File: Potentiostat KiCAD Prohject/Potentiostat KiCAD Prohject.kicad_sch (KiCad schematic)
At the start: 30 parts, among them K1 DIPxx-1Axx-12xD, U1 OPA2277, U2 TL074, U3 RP2040, U4 OPA2277, U5 INA128, U7 INA128, U8 REF3033, U9 INA128

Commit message: completed ESP32 design
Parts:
- removed U3: RP2040, Package_DFN_QFN:QFN-56-1EP_7x7mm_P0.4mm_EP3.2x3.2mm, symbol MCU_RaspberryPi:RP2040
- added J1: USB_B_Micro, symbol Connector:USB_B_Micro
- added U10: ADS1115IDGS, Package_SO:TSSOP-10_3x3mm_P0.5mm, symbol Analog_ADC:ADS1115IDGS
- added U11, U6: MCP4725xxx-xCH, Package_TO_SOT_SMD:SOT-23-6, symbol Analog_DAC:MCP4725xxx-xCH
- added U12: RT9080-33GJ5, TSOT-23-5_RIT, symbol 2025-04-04_01-18-31:RT9080-33GJ5
- added U3: ESP32-S2, Package_DFN_QFN:QFN-56-1EP_7x7mm_P0.4mm_EP4x4mm, symbol MCU_Espressif:ESP32-S2
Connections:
- net GND: now also U10.3 (GND), U11.2 (VSS), U3.57 (GND), U6.2 (VSS), U6.6 (A0)
- net goes to ADC: no longer names the net of R6.1, R7.1, U1.5 (+), U1.7
- net goes to ADC: now also U10.7 (AIN3); no longer D2.1 (K), U9.2 (-), U9.6
- net goes to DAC: no longer names the net of U1.6 (-)
- net goes to DAC: now also U6.1 (VOUT)
- net goes to MCU: no longer names the net of K1.7, K1.8
- net goes to MCU: now also U10.5 (AIN1); no longer R12.2, R5.1
- new net: R12.2, U3.17 (GPIO12)
- new net: D2.1 (K), U10.6 (AIN2), U9.2 (-), U9.6
- new net: R5.1, U11.1 (VOUT)
- new net: U10.9 (SDA), U11.4 (SDA), U3.13 (GPIO8), U6.4 (SDA)
- new net: U10.10 (SCL), U11.5 (SCL), U3.14 (GPIO9), U6.5 (SCL)
- new net: J1.1 (VBUS), U12.1 (VIN)
- new net: J1.2 (D-), U3.25 (GPIO19/USB_D-)
- new net: J1.3 (D+), U3.26 (GPIO20/USB_D+)
- new net: J1.5 (GND), U12.2 (GND)
- new net: U12.5 (VOUT), U3.45 (VDD3P3_CPU)
- new net: U3.1 (VDDA), U3.51 (VDDA), U3.54 (VDDA)
- new net: U3.3 (VDD3P3), U3.4 (VDD3P3)
- new net VCC: U10.8 (VDD), U11.3 (VDD), U11.6 (A0), U6.3 (VDD)

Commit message: add microcontroller stuff
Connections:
- net GND: now also J1.5 (GND), U12.2 (GND)
- net at U12.5 (VOUT): now also U3.3 (VDD3P3), U3.4 (VDD3P3); no longer U3.45 (VDD3P3_CPU)
- no-connect marks 12 -> 65

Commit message: esp32 solo and cleanup
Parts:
- removed J1: USB_B_Micro, symbol Connector:USB_B_Micro
- removed U12: RT9080-33GJ5, TSOT-23-5_RIT, symbol 2025-04-04_01-18-31:RT9080-33GJ5
- removed U3: ESP32-S2, Package_DFN_QFN:QFN-56-1EP_7x7mm_P0.4mm_EP4x4mm, symbol MCU_Espressif:ESP32-S2
- added C2: 100nF, Capacitor_SMD:C_0805_2012Metric_Pad1.18x1.45mm_HandSolder, symbol Device:C
- added C3: 10uF, Capacitor_SMD:C_0805_2012Metric_Pad1.18x1.45mm_HandSolder, symbol Device:C
- added C4, C6: .1uF, Capacitor_SMD:C_0805_2012Metric_Pad1.18x1.45mm_HandSolder, symbol Device:C
- added C5: 1uF, Capacitor_SMD:C_0805_2012Metric_Pad1.18x1.45mm_HandSolder, symbol Device:C
- added J2: USB_C_Receptacle_USB2.0, Connector_USB:USB_C_Receptacle_GCT_USB4105-xx-A_16P_TopMnt_Horizontal, symbol Connector:USB_C_Receptacle_USB2.0
- added R19, R20: 5.1 k, Resistor_SMD:R_0805_2012Metric_Pad1.20x1.40mm_HandSolder, symbol Device:R
- added R21: 10k, Resistor_SMD:R_0805_2012Metric_Pad1.20x1.40mm_HandSolder, symbol Device:R
- added SW1: Reset, symbol Switch:SW_Omron_B3FS
- added SW2: Boot, symbol Switch:SW_Omron_B3FS
- added U13: LD1117S33TR_SOT223, Package_TO_SOT_SMD:SOT-223-3_TabPin2, symbol Regulator_Linear:LD1117S33TR_SOT223
- added U14: ESP32-S2-SOLO, PCM_Espressif:ESP32-S2-SOLO, symbol esp32:ESP32-S2-SOLO
- C1: footprint (none) -> B58031I7504M062:CAPC7851084X4N
- D1: footprint (none) -> LED_SMD:LED_0603_1608Metric
- R1, R10, R11, R13, R14, R15, R16, R17, R18, R2, R3, R4, R5, R6, R7, R8, R9: footprint (none) -> Resistor_THT:R_Axial_DIN0207_L6.3mm_D2.5mm_P7.62mm_Horizontal
- R12: footprint (none) -> footprints:res2_1-1625885-7_TEC
- U1, U4, U5, U7, U9: footprint (none) -> Package_SO:SOIC-8_3.9x4.9mm_P1.27mm
- U2: footprint (none) -> Package_SO:SOIC-14_3.9x8.7mm_P1.27mm
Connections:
- net GND: now also C2.2, C3.2, C4.1, C5.2, C6.2, J2.A1 (GND), J2.A12 (GND), J2.B1 (GND), J2.B12 (GND), J2.S1 (SHIELD), R19.2, R20.1, SW1.1, SW2.2, U13.1 (GND), U14.1 (GND), U14.40 (GND), U14.41 (GND)
- net at R12.2: now also U14.20 (GPIO12/TOUCH12/ADC2_CH1/FSPICLK/FSPIIO6)
- net at R13.2, R15.2, R16.1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: now also R14.1; no longer R14.2
- net I2C_SDA: now reaches U10.9 (SDA), U11.4 (SDA), U6.4 (SDA)
- net I2C_SDA: now also U14.17 (GPIO9/TOUCH9/ADC1_CH8/FSPIHD)
- net I2C_SCL: now reaches U10.10 (SCL), U11.5 (SCL), U6.5 (SCL)
- net I2C_SCL: now also U14.12 (GPIO8/TOUCH8/ADC1_CH7)
- net at R6.1, R7.1, U1.5 (+)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: no longer U10.7 (AIN3)
- net at R13.1, U7.6, U9.3 (+): now also R14.2; no longer R14.1
- new net: C4.2, R21.2, SW1.2, U14.3 (EN)
- new net: SW2.1, U14.27 (GPIO0)
- new net: J2.A5 (CC1), R19.1
- new net: J2.B5 (CC2), R20.2
- new net +3.3V: C3.1, C5.1, C6.1, R21.1, U13.2 (VO), U14.2 (3V3)
- new net +5V: C2.1, J2.A4 (VBUS), J2.A9 (VBUS), J2.B4 (VBUS), J2.B9 (VBUS), U13.3 (VI)
- new net D+: J2.A6 (D+), J2.B6 (D+), U14.14 (GPIO20/U1CTS/ADC2_CH9/CLK_OUT1/USB_D+)
- new net D-: J2.A7 (D-), J2.B7 (D-), U14.13 (GPIO19/U1RTS/ADC2_CH8/CLK_OUT2/USB_D-)
- no-connect marks 65 -> 17
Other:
- note added: "3.3V Supply"
- note added: "ESP32S2"
- note added: "USB_Connector"
- moved on the sheet: D1, R12, R14, U11, U2A, U2B, U2C, U2E, U6

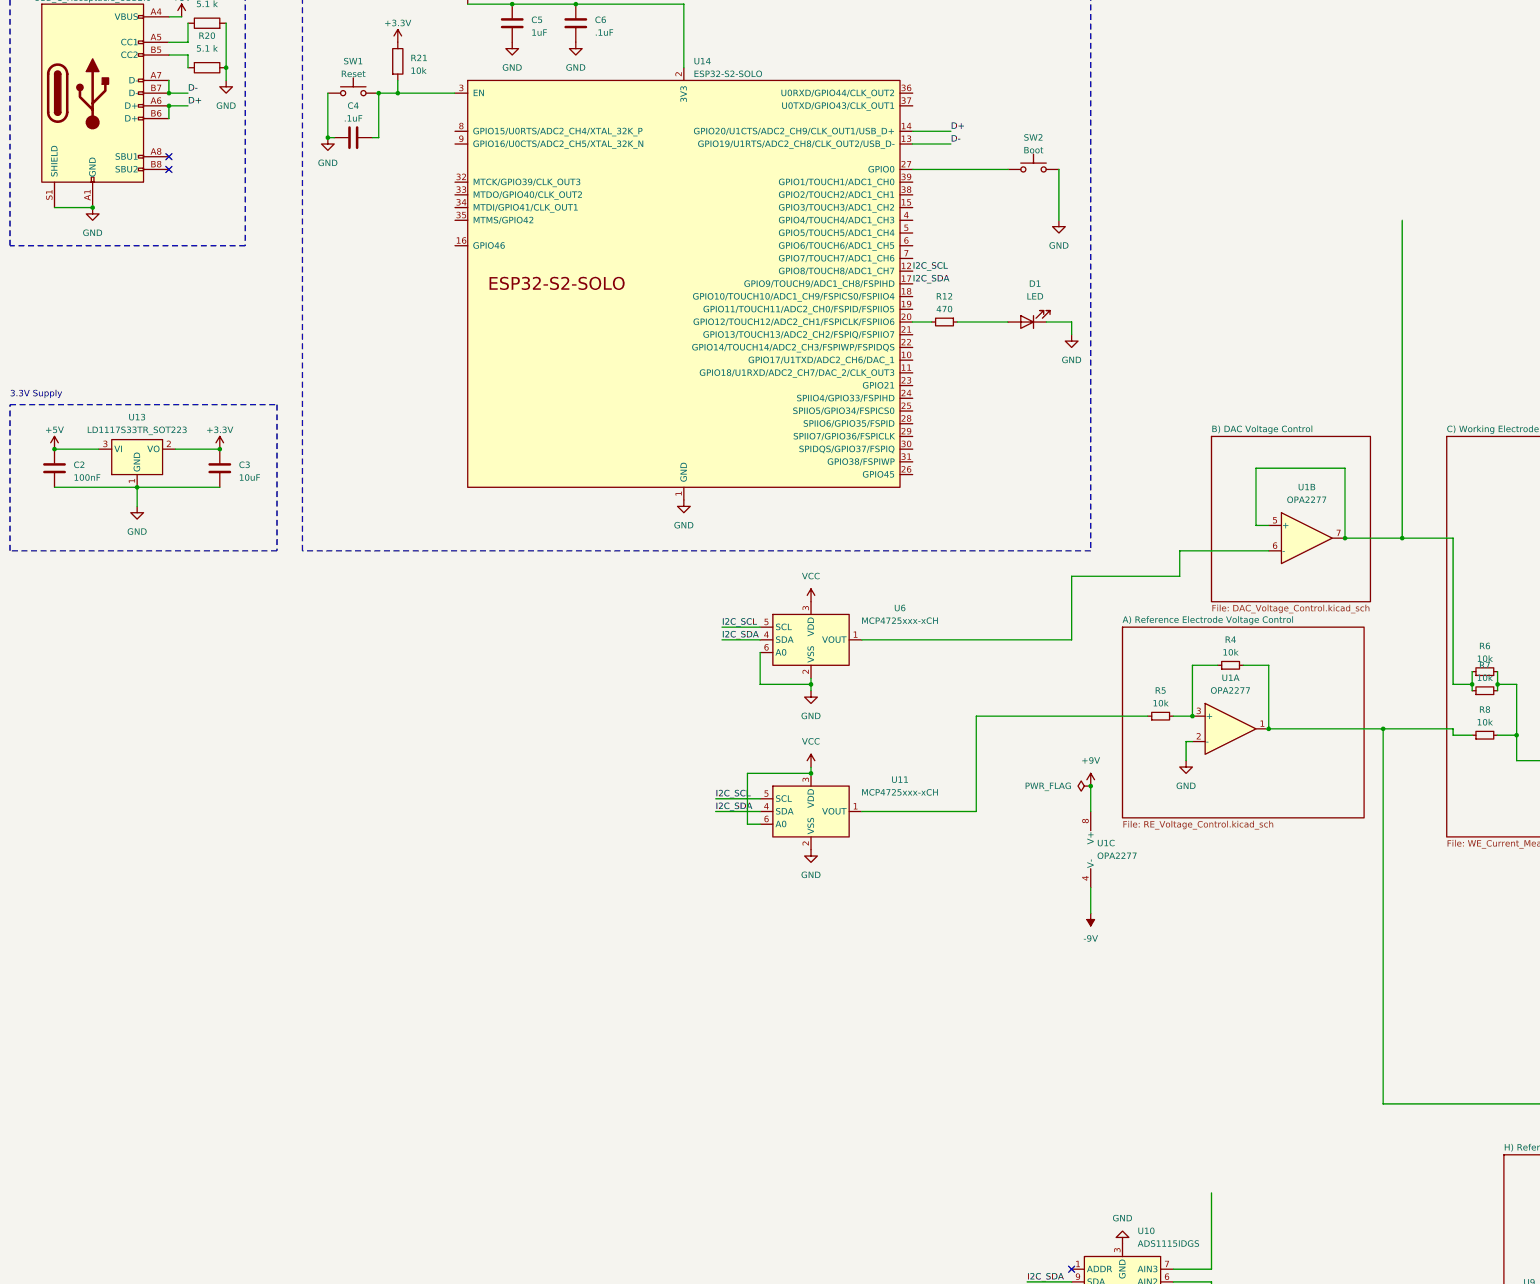
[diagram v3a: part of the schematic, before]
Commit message: updated wires
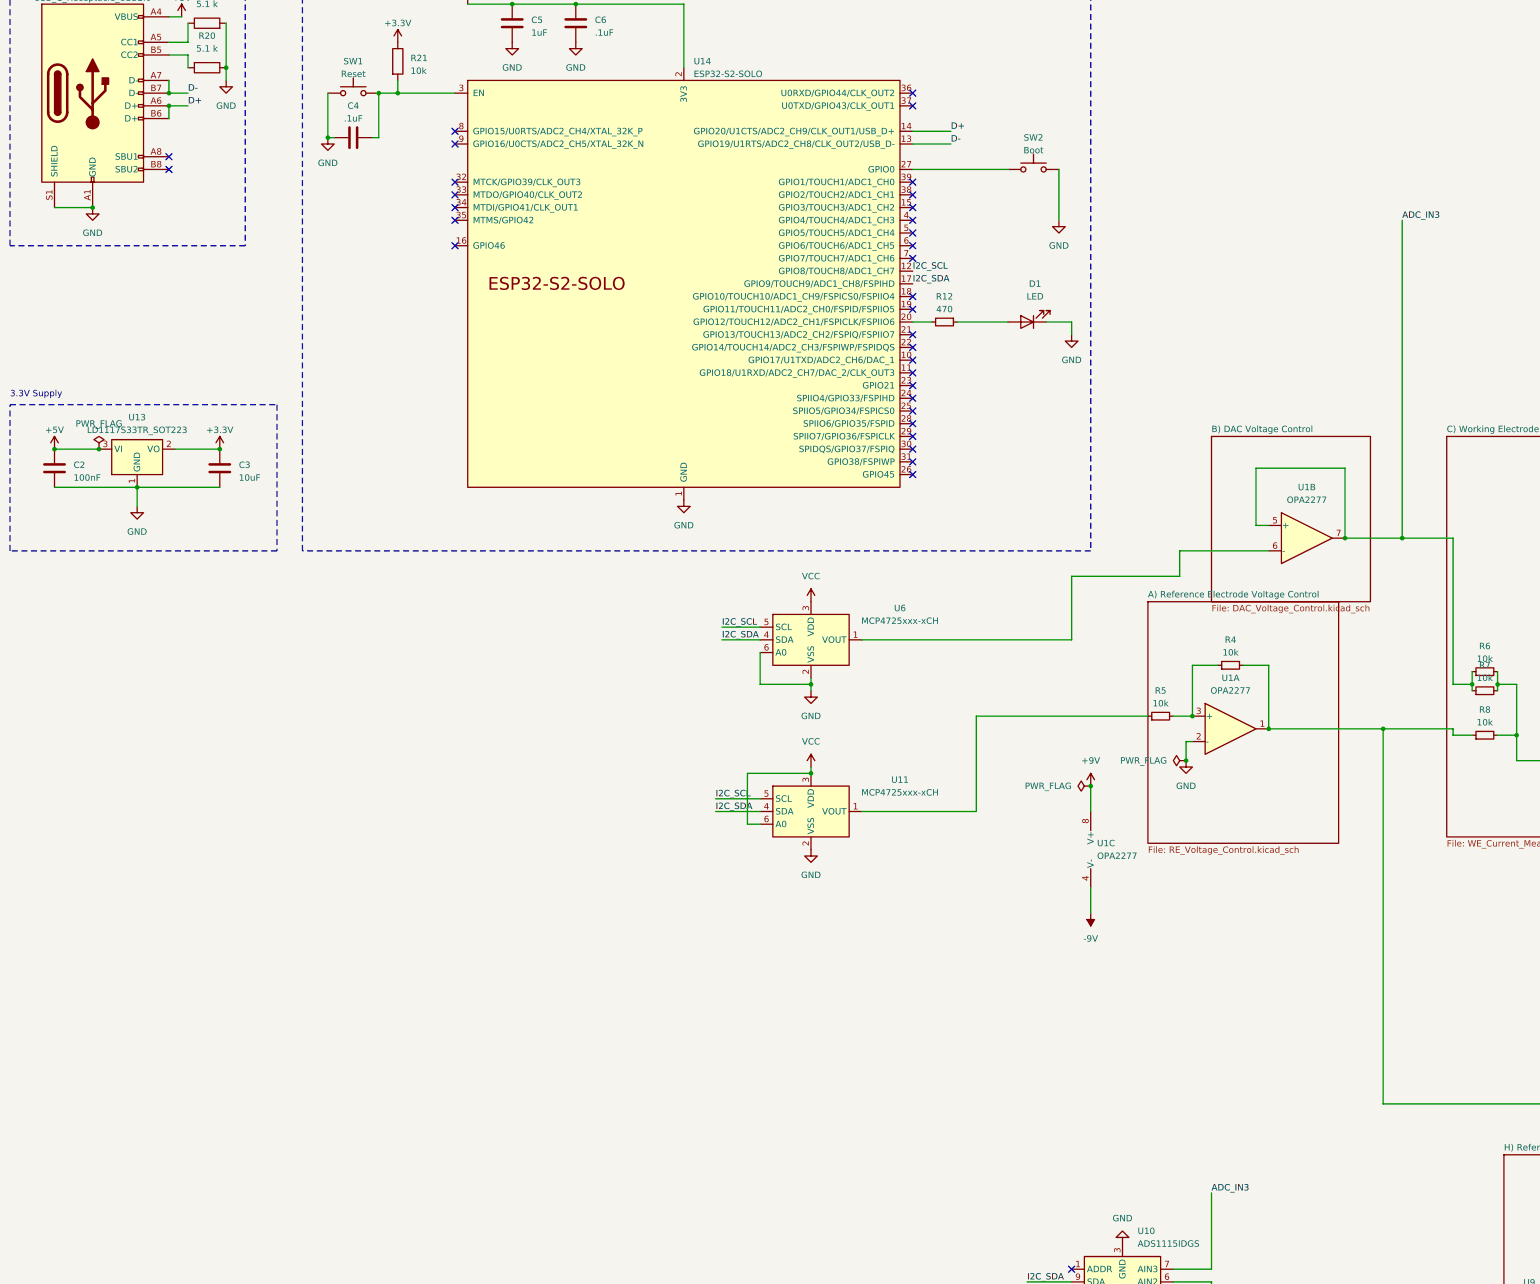
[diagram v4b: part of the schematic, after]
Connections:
- net ADC_IN3: now reaches U10.7 (AIN3)
- net ADC_IN3: now also R6.1, R7.1, U1.5 (+), U1.7
- no-connect marks 17 -> 47
